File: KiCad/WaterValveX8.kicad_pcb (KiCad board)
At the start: 2 copper layers, 66.7 x 42.3 mm, 82 parts, among them J10 Screw_Terminal_01x03, J2 Conn_01x03_Male, J3 Screw_Terminal_01x02, J4 Conn_01x01_Male, J5 Screw_Terminal_01x03, J6 Conn_01x04_Male, J7 Screw_Terminal_01x03, J8 Screw_Terminal_01x03, J9 Screw_Terminal_01x03, Q1 IRLML2502, Q2 IRLML2502, Q3 IRLML2502, Q4 IRLML2502, Q5 IRLML2502, Q6 IRLML2502, Q7 IRLML2502, Q8 IRLML2502, U1 L7805, U2 XIAO-ESP32-C6-SMD, U3 TPS561201/08 or TPS563200

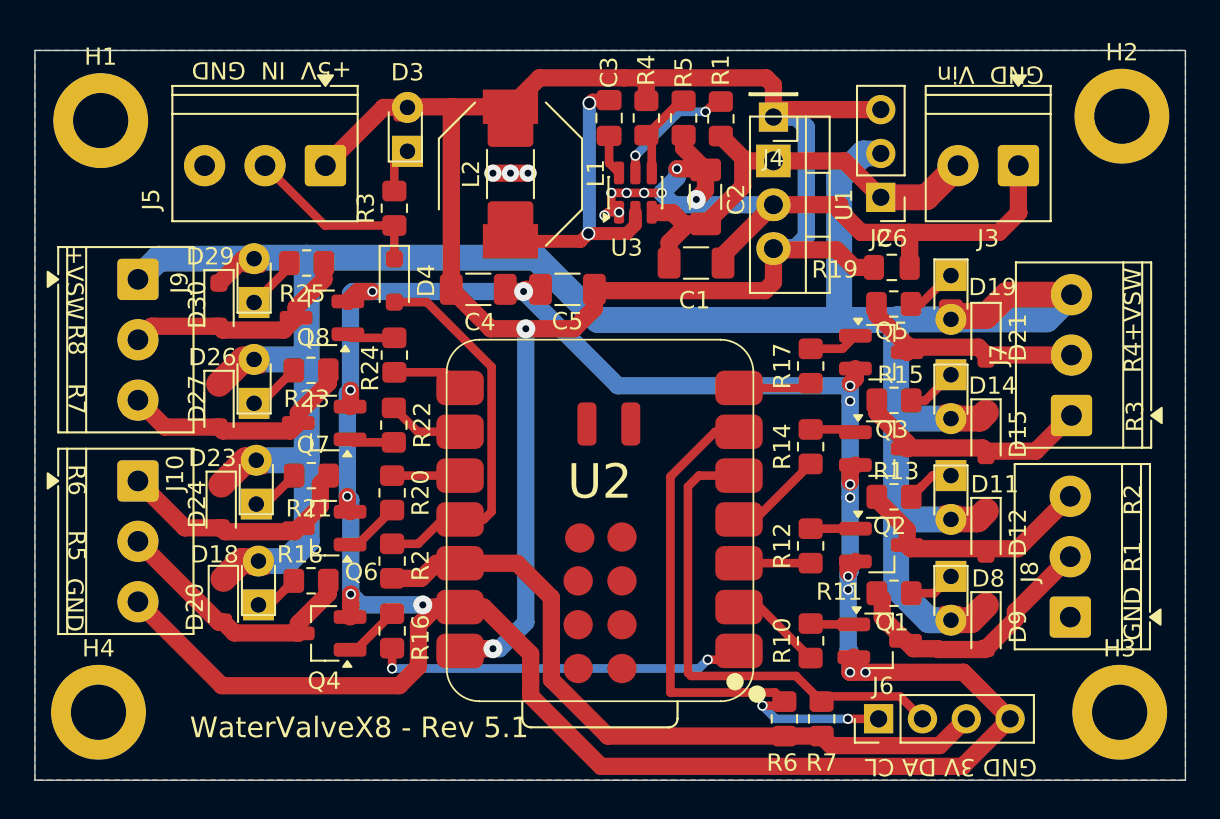
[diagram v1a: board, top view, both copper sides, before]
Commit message: DRC and bump to version 5.2
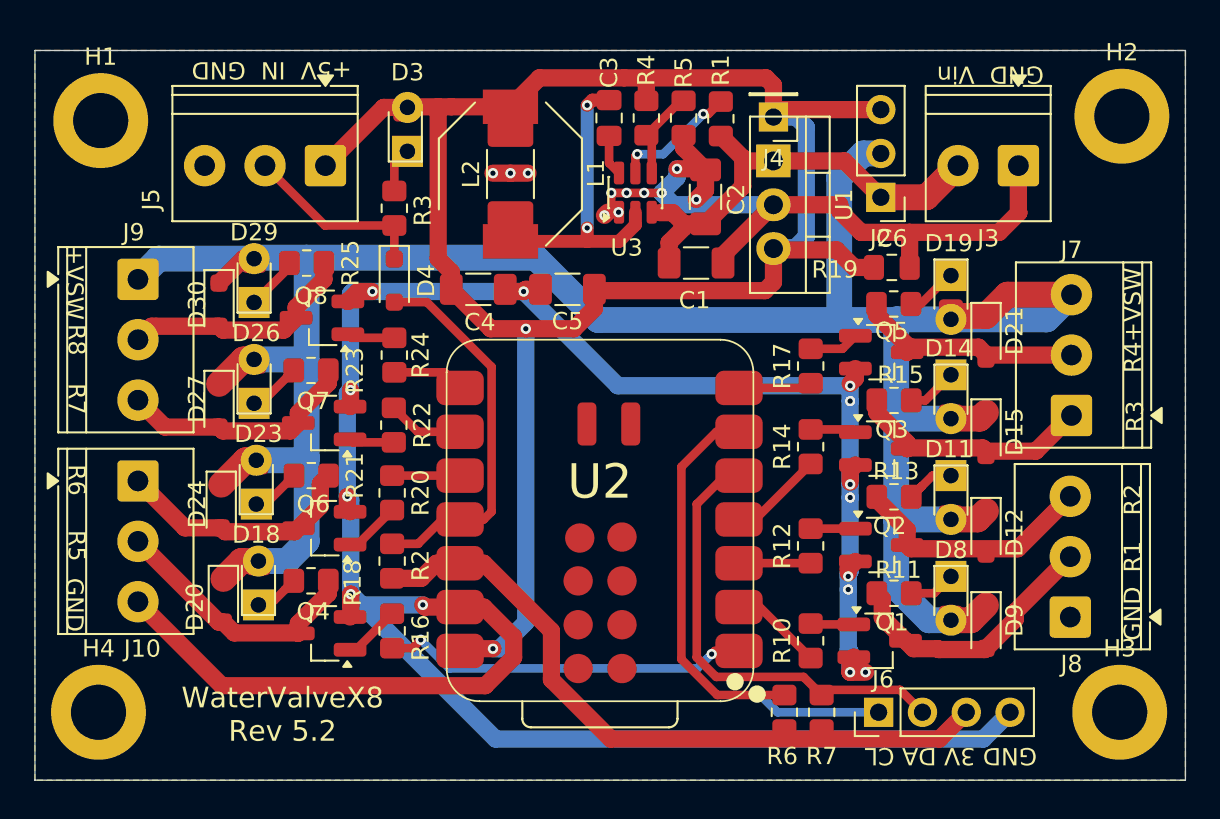
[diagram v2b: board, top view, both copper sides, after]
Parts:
- moved J6 0.38 mm to (184.8, 119.9)
- moved R6 0.38 mm to (179.3, 119.9)
- moved R7 0.38 mm to (181.5, 119.9)
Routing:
- net /SCL: track 32.8 -> 29.4 mm, vias 2 -> 1
- net /SDA: track 29.0 -> 26.7 mm
- net +3V3: track 41.4 -> 40.2 mm
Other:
- board text added: "WaterValveX8 Rev 5.2"
- board text removed: "WaterValveX8 - Rev 5.1"
